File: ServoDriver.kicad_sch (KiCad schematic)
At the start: 1 part, among them U3 ATtiny85-20P

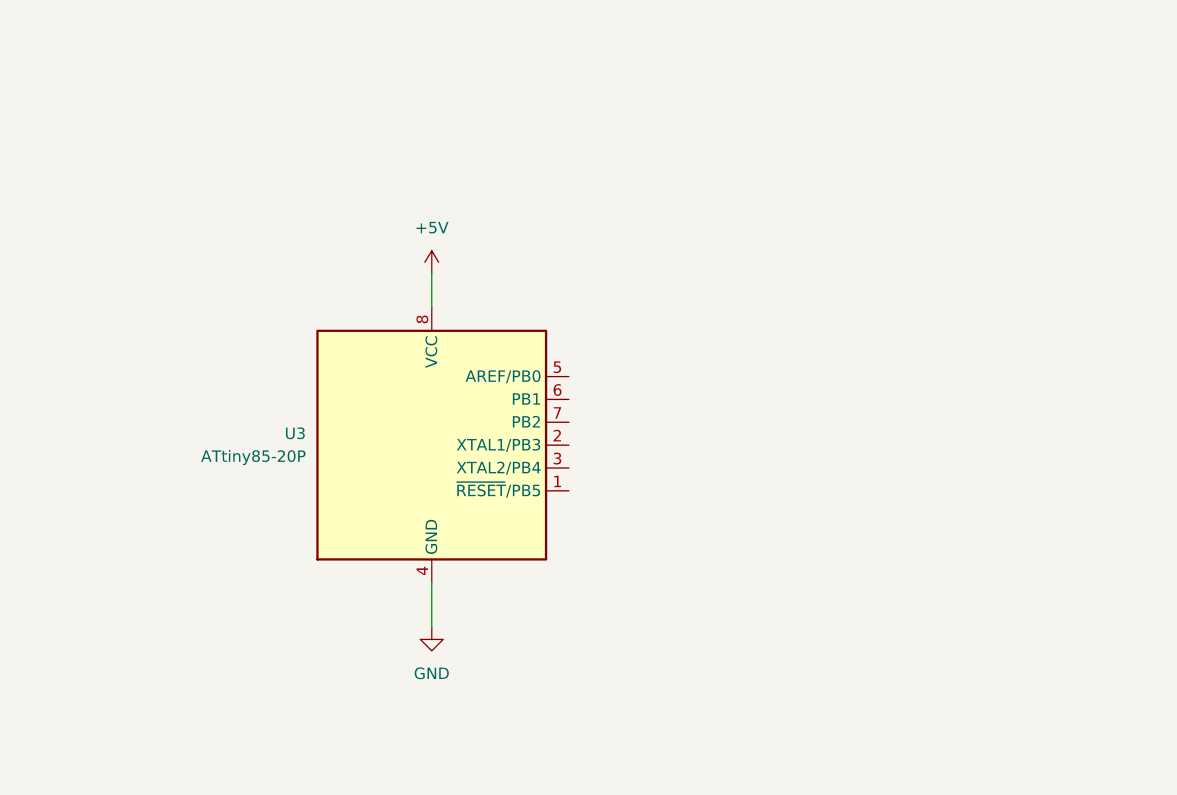
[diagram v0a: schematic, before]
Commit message: ServoDriver schematic
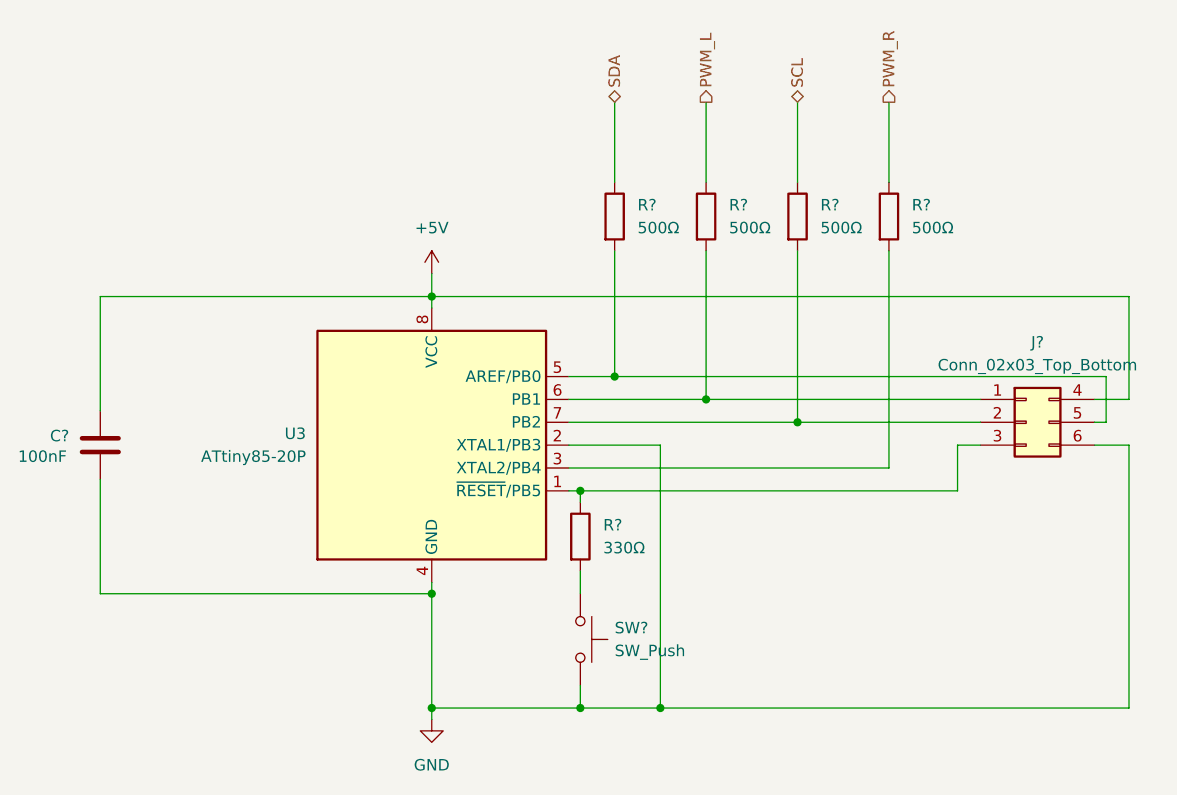
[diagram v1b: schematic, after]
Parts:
- added C?: 100nF, symbol Device:C
- added J?: Conn_02x03_Top_Bottom, symbol Connector_Generic:Conn_02x03_Top_Bottom
- added R? (x4): 500Ω, symbol Device:R
- added R?: 330Ω, symbol Device:R
- added SW?: SW_Push, symbol Switch:SW_Push
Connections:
- net +5V: now also C?.1, J?.4 (Pin_4)
- net GND: now also U3.2 (XTAL1/PB3), C?.2, J?.6 (Pin_6), SW?.2
- net at U3.1 (~{RESET}/PB5): now also J?.3 (Pin_3), R?.1
- net at U3.3 (XTAL2/PB4): now also R?.2
- net at U3.5 (AREF/PB0): now also J?.5 (Pin_5), R?.2
- net at U3.6 (PB1): now also J?.1 (Pin_1), R?.2
- net at U3.7 (PB2): now also J?.2 (Pin_2), R?.2
- new net: R?.2, SW?.1
- new net PWM_L: R?.1
- new net PWM_R: R?.1
- new net SCL: R?.1
- new net SDA: R?.1

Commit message: HBridge top file connections (NOT CONNECTED TO TOP FILE YET)
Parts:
- gave numbers to parts that had none: 8
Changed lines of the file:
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@@
 		(dnp no)
 		(fields_autoplaced yes)
-		(property "Reference" "#PWR05"
+		(property "Reference" "#PWR06"
 			(at 148.59 80.01 0)
 			(effects
@@
 			(project ""
 				(path "/8372e765-ead7-42d0-82da-59a3937ad504/246fcda0-ab8f-4d1b-9427-9837f3ddf225"
-					(reference "#PWR05")
+					(reference "#PWR06")
 					(unit 1)
 				)
@@
 		(on_board yes)
 		(dnp no)
-		(property "Reference" "C?"
+		(property "Reference" "C3"
 			(at 106.172 94.234 0)
 			(effects
@@
 			(project "PAFT_pcbs"
 				(path "/8372e765-ead7-42d0-82da-59a3937ad504/246fcda0-ab8f-4d1b-9427-9837f3ddf225"
-					(reference "C?")
+					(reference "C3")
 					(unit 1)
 				)
@@
 		(dnp no)
 		(fields_autoplaced yes)
-		(property "Reference" "R?"
+		(property "Reference" "R5"
 			(at 181.61 68.5799 0)
 			(effects
@@
 			(project "PAFT_pcbs"
 				(path "/8372e765-ead7-42d0-82da-59a3937ad504/246fcda0-ab8f-4d1b-9427-9837f3ddf225"
-					(reference "R?")
+					(reference "R5")
 					(unit 1)
 				)
@@
 		(dnp no)
 		(fields_autoplaced yes)
-		(property "Reference" "SW?"
+		(property "Reference" "SW1"
 			(at 168.91 115.5699 90)
 			(effects
@@
 			(project "PAFT_pcbs"
 				(path "/8372e765-ead7-42d0-82da-59a3937ad504/246fcda0-ab8f-4d1b-9427-9837f3ddf225"
-					(reference "SW?")
+					(reference "SW1")
 					(unit 1)
 				)
@@
 		(dnp no)
 		(fields_autoplaced yes)
-		(property "Reference" "J?"
+		(property "Reference" "J3"
 			(at 215.9 83.82 0)
 			(effects
@@
 			(project "PAFT_pcbs"
 				(path "/8372e765-ead7-42d0-82da-59a3937ad504/246fcda0-ab8f-4d1b-9427-9837f3ddf225"
-					(reference "J?")
+					(reference "J3")
 					(unit 1)
 				)
@@
 		(dnp no)
 		(fields_autoplaced yes)
-		(property "Reference" "R?"
+		(property "Reference" "R3"
 			(at 167.64 104.1399 0)
 			(effects
@@
 			(project "PAFT_pcbs"
 				(path "/8372e765-ead7-42d0-82da-59a3937ad504/246fcda0-ab8f-4d1b-9427-9837f3ddf225"
-					(reference "R?")
+					(reference "R3")
 					(unit 1)
 				)
@@
 		(dnp no)
 		(fields_autoplaced yes)
-		(property "Reference" "R?"
+		(property "Reference" "R4"
 			(at 171.45 68.5799 0)
 			(effects
@@
 			(project "PAFT_pcbs"
 				(path "/8372e765-ead7-42d0-82da-59a3937ad504/246fcda0-ab8f-4d1b-9427-9837f3ddf225"
-					(reference "R?")
+					(reference "R4")
 					(unit 1)
 				)
@@
 		(dnp no)
 		(fields_autoplaced yes)
-		(property "Reference" "R?"
+		(property "Reference" "R7"
 			(at 201.93 68.5799 0)
 			(effects
@@
 			(project "PAFT_pcbs"
 				(path "/8372e765-ead7-42d0-82da-59a3937ad504/246fcda0-ab8f-4d1b-9427-9837f3ddf225"
-					(reference "R?")
+					(reference "R7")
 					(unit 1)
 				)
@@
 		(dnp no)
 		(fields_autoplaced yes)
-		(property "Reference" "R?"
+		(property "Reference" "R6"
 			(at 191.77 68.5799 0)
 			(effects
@@
 			(project "PAFT_pcbs"
 				(path "/8372e765-ead7-42d0-82da-59a3937ad504/246fcda0-ab8f-4d1b-9427-9837f3ddf225"
-					(reference "R?")
+					(reference "R6")
 					(unit 1)
 				)
@@
 		(dnp no)
 		(fields_autoplaced yes)
-		(property "Reference" "#PWR04"
+		(property "Reference" "#PWR07"
 			(at 148.59 132.08 0)
 			(effects
@@
 			(project ""
 				(path "/8372e765-ead7-42d0-82da-59a3937ad504/246fcda0-ab8f-4d1b-9427-9837f3ddf225"
-					(reference "#PWR04")
-					(unit 1)
-				)
+					(reference "#PWR07")
+					(unit 1)
+				)

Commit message: Updated schematic
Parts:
- J3: footprint (none) -> Connector_PinHeader_2.54mm:PinHeader_2x03_P2.54mm_Vertical
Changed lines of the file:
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@@
 			)
 		)
-		(property "Footprint" ""
+		(property "Footprint" "Connector_PinHeader_2.54mm:PinHeader_2x03_P2.54mm_Vertical"
 			(at 214.63 92.71 0)
 			(effects

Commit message: Added footprints
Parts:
- C3: footprint (none) -> Capacitor_SMD:C_0805_2012Metric
- R3: value 330Ω -> 500Ω; footprint (none) -> Resistor_SMD:R_0805_2012Metric
- R4, R5, R6, R7: footprint (none) -> Resistor_SMD:R_0805_2012Metric
- SW1: footprint (none) -> Button_Switch_THT:SW_PUSH_6mm_H4.3mm
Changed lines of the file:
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@@
 			)
 		)
-		(property "Footprint" ""
+		(property "Footprint" "Capacitor_SMD:C_0805_2012Metric"
 			(at 112.7252 99.06 0)
 			(effects
@@
 			)
 		)
-		(property "Footprint" ""
+		(property "Footprint" "Resistor_SMD:R_0805_2012Metric"
 			(at 177.292 69.85 90)
 			(effects
@@
 			)
 		)
-		(property "Footprint" ""
+		(property "Footprint" "Button_Switch_THT:SW_PUSH_6mm_H4.3mm"
 			(at 170.18 116.84 0)
 			(effects
@@
 			)
 		)
-		(property "Value" "330Ω"
+		(property "Value" "500Ω"
 			(at 167.64 106.6799 0)
 			(effects
@@
 			)
 		)
-		(property "Footprint" ""
+		(property "Footprint" "Resistor_SMD:R_0805_2012Metric"
 			(at 163.322 105.41 90)
 			(effects
@@
 			)
 		)
-		(property "Footprint" ""
+		(property "Footprint" "Resistor_SMD:R_0805_2012Metric"
 			(at 167.132 69.85 90)
 			(effects
@@
 			)
 		)
-		(property "Footprint" ""
+		(property "Footprint" "Resistor_SMD:R_0805_2012Metric"
 			(at 197.612 69.85 90)
 			(effects
@@
 			)
 		)
-		(property "Footprint" ""
+		(property "Footprint" "Resistor_SMD:R_0805_2012Metric"
 			(at 187.452 69.85 90)
 			(effects

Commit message: PCB Placement and Planes
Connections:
- net GND: no longer U3.2 (XTAL1/PB3)
- no-connect marks 0 -> 1
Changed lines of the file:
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@@
-	)
-	(junction
-		(at 173.99 124.46)
-		(diameter 0)
-		(color 0 0 0 0)
 	)
 	(junction
@@
 		(color 0 0 0 0)
 	)
+	(no_connect
+		(at 163.83 95.25)
+	)
 	(wire
 		(pts
@@
 	(wire
 		(pts
-			(xy 173.99 95.25) (xy 173.99 124.46)
-		)
-		(stroke
-			(width 0)
-			(type default)
-		)
-	)
-	(wire
-		(pts
 			(xy 165.1 109.22) (xy 165.1 111.76)
 		)
@@
 	(wire
 		(pts
-			(xy 226.06 124.46) (xy 173.99 124.46)
+			(xy 165.1 124.46) (xy 226.06 124.46)
 		)
 		(stroke
@@
 		)
 		(stroke
-			(width 0)
-			(type default)
-		)
-	)
-	(wire
-		(pts
-			(xy 173.99 124.46) (xy 165.1 124.46)
-		)
-		(stroke
-			(width 0)
-			(type default)
-		)
-	)
-	(wire
-		(pts
-			(xy 163.83 95.25) (xy 173.99 95.25)
-		)
-		(stroke

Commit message: Routing adjustments
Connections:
- net GND: now also U3.2 (XTAL1/PB3)
- no-connect marks 1 -> 0
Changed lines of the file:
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@@
+	)
+	(junction
+		(at 181.61 124.46)
+		(diameter 0)
+		(color 0 0 0 0)
 	)
 	(junction
@@
 		(color 0 0 0 0)
 	)
-	(no_connect
-		(at 163.83 95.25)
-	)
 	(wire
 		(pts
@@
 	(wire
 		(pts
+			(xy 163.83 95.25) (xy 181.61 95.25)
+		)
+		(stroke
+			(width 0)
+			(type default)
+		)
+	)
+	(wire
+		(pts
 			(xy 179.07 57.15) (xy 179.07 66.04)
 		)
@@
 	(wire
 		(pts
-			(xy 165.1 124.46) (xy 226.06 124.46)
+			(xy 165.1 124.46) (xy 181.61 124.46)
 		)
 		(stroke
@@
 	(wire
 		(pts
+			(xy 181.61 124.46) (xy 226.06 124.46)
+		)
+		(stroke
+			(width 0)
+			(type default)
+		)
+	)
+	(wire
+		(pts
 			(xy 163.83 97.79) (xy 199.39 97.79)
 		)
@@
 		)
 		(stroke
+			(width 0)
+			(type default)
+		)
+	)
+	(wire
+		(pts
+			(xy 181.61 95.25) (xy 181.61 124.46)
+		)
+		(stroke
